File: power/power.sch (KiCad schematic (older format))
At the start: 81 parts, among them J1 Conn_01x02_Female, J2 Conn_01x02_Female, J3 CONN_02X03, J4 Conn_01x06_Female, Q1 BS170, Q10 BS170, Q11 BS170, Q12 BSB014N04LX3, Q2 BS170, Q3 BS170, Q4 BS170, Q5 BS170, Q6 BS170, Q7 BS170, Q8 BS170, Q9 BS170, U1 MAX1648, U2 TPS2592xx, U3 LMC6482, U4 ATSAMD21G18A-AUT

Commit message: added to sch
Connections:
- wire segments 190 -> 187
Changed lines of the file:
@@
 	1    0    0    -1
 $EndComp
-Text Label 10650 1850 0    50   ~ 0
+Text Label 11000 1850 0    50   ~ 0
 T2
 Text Label 9650 1750 2    50   ~ 0
@@
 Text Label 750  6700 2    50   ~ 0
 BAT-
-Text Label 10650 2650 0    50   ~ 0
+Text Label 11000 2650 0    50   ~ 0
 FET1
 Text Label 9650 3050 2    50   ~ 0
 Discharge
-Text Label 10650 2750 0    50   ~ 0
+Text Label 11000 2750 0    50   ~ 0
 FET2
-Text Label 10650 2850 0    50   ~ 0
+Text Label 11000 2850 0    50   ~ 0
 FET3
-Text Label 10650 2950 0    50   ~ 0
+Text Label 11000 2950 0    50   ~ 0
 FET4
 Text Label 9650 3350 2    50   ~ 0
@@
 Connection ~ 6850 6700
 Connection ~ 6850 3950
-Text Label 10650 1950 0    50   ~ 0
+Text Label 11000 1950 0    50   ~ 0
 T1
 $Comp
@@
 	1    0    0    -1
 $EndComp
-Wire Wire Line
-	10150 3850 10250 3850
-Connection ~ 10250 3850
-Wire Wire Line
-	10250 3850 10350 3850
-Connection ~ 10350 3850
-Wire Wire Line
-	10350 3850 10450 3850
-Connection ~ 10450 3850
-Wire Wire Line
-	10450 3850 10700 3850
 Text Label 7150 6700 0    50   ~ 0
 LOAD-
@@
 Text Label 4250 6300 2    50   ~ 0
 SafetySwitch
-Text Label 10650 2050 0    50   ~ 0
+Text Label 11000 2050 0    50   ~ 0
 SafetySwitch
 NoConn ~ 9650 1350
@@
 NoConn ~ 9650 3150
 NoConn ~ 9650 3250
-NoConn ~ 10650 2550
-NoConn ~ 10650 2450
-NoConn ~ 10650 2350
-NoConn ~ 10650 2250
-NoConn ~ 10650 2150
-NoConn ~ 10650 1750
-NoConn ~ 10650 1650
-NoConn ~ 10650 1550
-NoConn ~ 10650 1450
-Wire Wire Line
-	10050 850  10150 850
-Connection ~ 10150 850
-Wire Wire Line
-	10150 850  10250 850
-Connection ~ 10250 850
-Wire Wire Line
-	10250 850  10350 850
-Connection ~ 10350 850
-Wire Wire Line
-	10350 850  10450 850
-Connection ~ 10450 850
-Wire Wire Line
-	10450 850  10650 850
+NoConn ~ 11000 2550
+NoConn ~ 11000 2450
+NoConn ~ 11000 2350
+NoConn ~ 11000 2250
+NoConn ~ 11000 2150
+NoConn ~ 11000 1750
+NoConn ~ 11000 1650
+NoConn ~ 11000 1550
+NoConn ~ 11000 1450
 $Comp
 L power:VCC #PWR0116
@@
 	-1   0    0    1
 $EndComp
+Wire Wire Line
+	10450 3850 10700 3850
+Wire Wire Line
+	10450 850  10650 850
+Wire Wire Line
+	10050 850  10150 850
+Connection ~ 10450 850
+Connection ~ 10150 850
+Wire Wire Line
+	10150 850  10250 850
+Connection ~ 10250 850
+Wire Wire Line
+	10250 850  10350 850
+Connection ~ 10350 850
+Wire Wire Line
+	10350 850  10450 850
 $EndSCHEMATC

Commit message: changed to atmega16
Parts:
- removed C15: C, Capacitor_SMD:C_0805_2012Metric_Pad1.15x1.40mm_HandSolder, symbol Device:C
- removed U4: ATSAMD21G18A-AUT, footprints:TO-263-2-Heatsink, symbol dk_Embedded-Microcontrollers:ATSAMD21G18A-AUT
- added C?: C, Capacitor_SMD:C_0805_2012Metric_Pad1.15x1.40mm_HandSolder, symbol Device:C
- added D?: D_Zener, symbol Device:D_Zener
- added U?: ATMEGA16M1, footprints:TQFP-32_7x7mm_Pitch0.8mm, symbol formula:ATMEGA16M1
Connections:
- net labels added: +3.3V
- wire segments 187 -> 191
- no-connect marks 24 -> 12
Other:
- moved on the sheet: C16, C17, D7, J4, Q10, Q9, R24, R25, R26, R27, R28, R29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

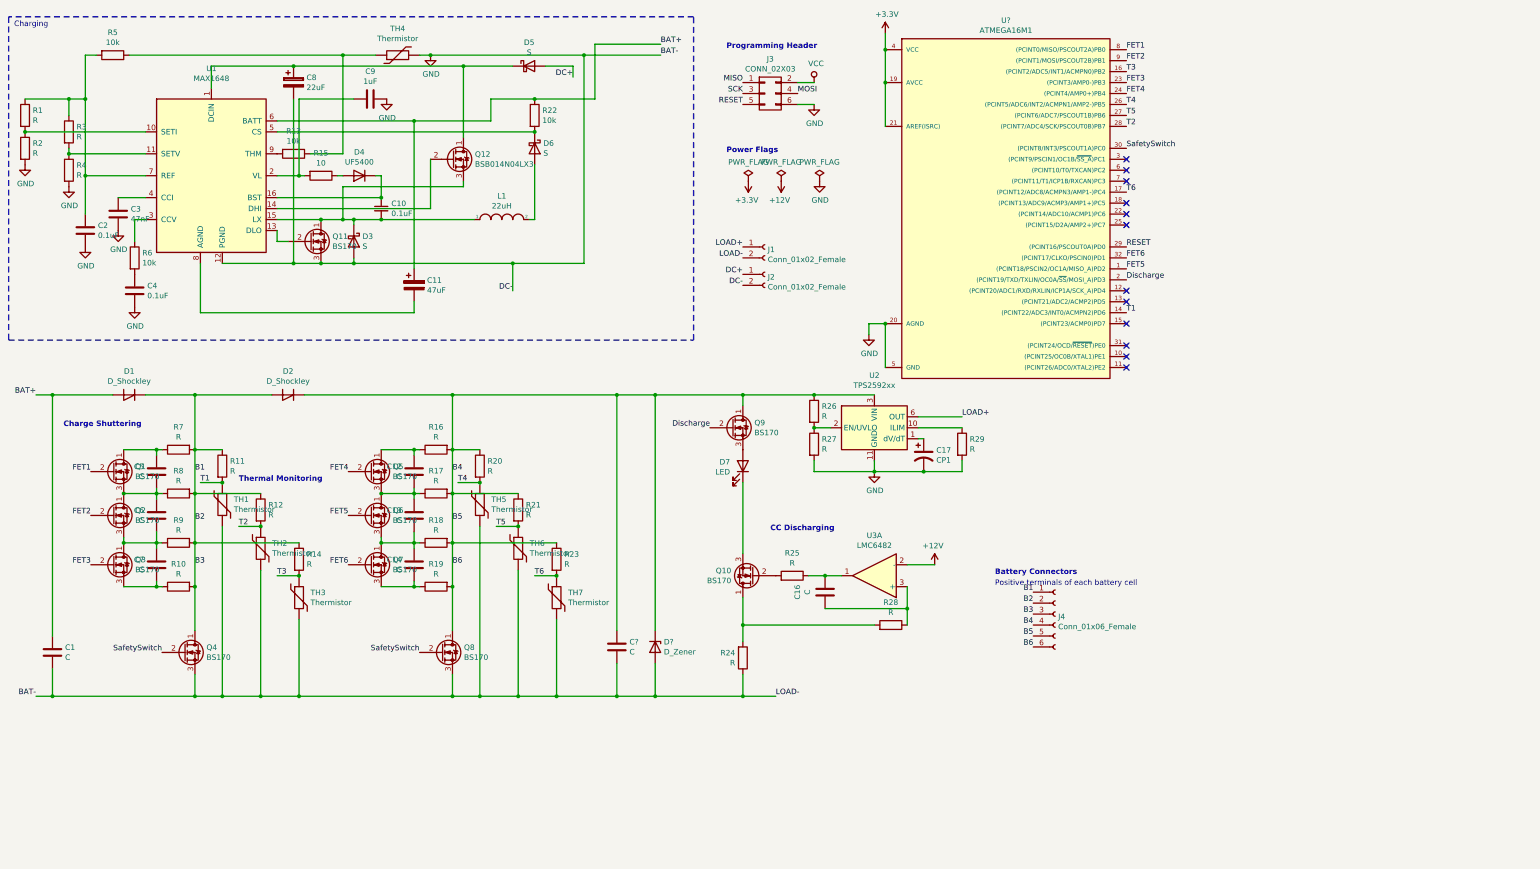
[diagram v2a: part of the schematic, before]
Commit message: Proper atmega configuration with programming header pins
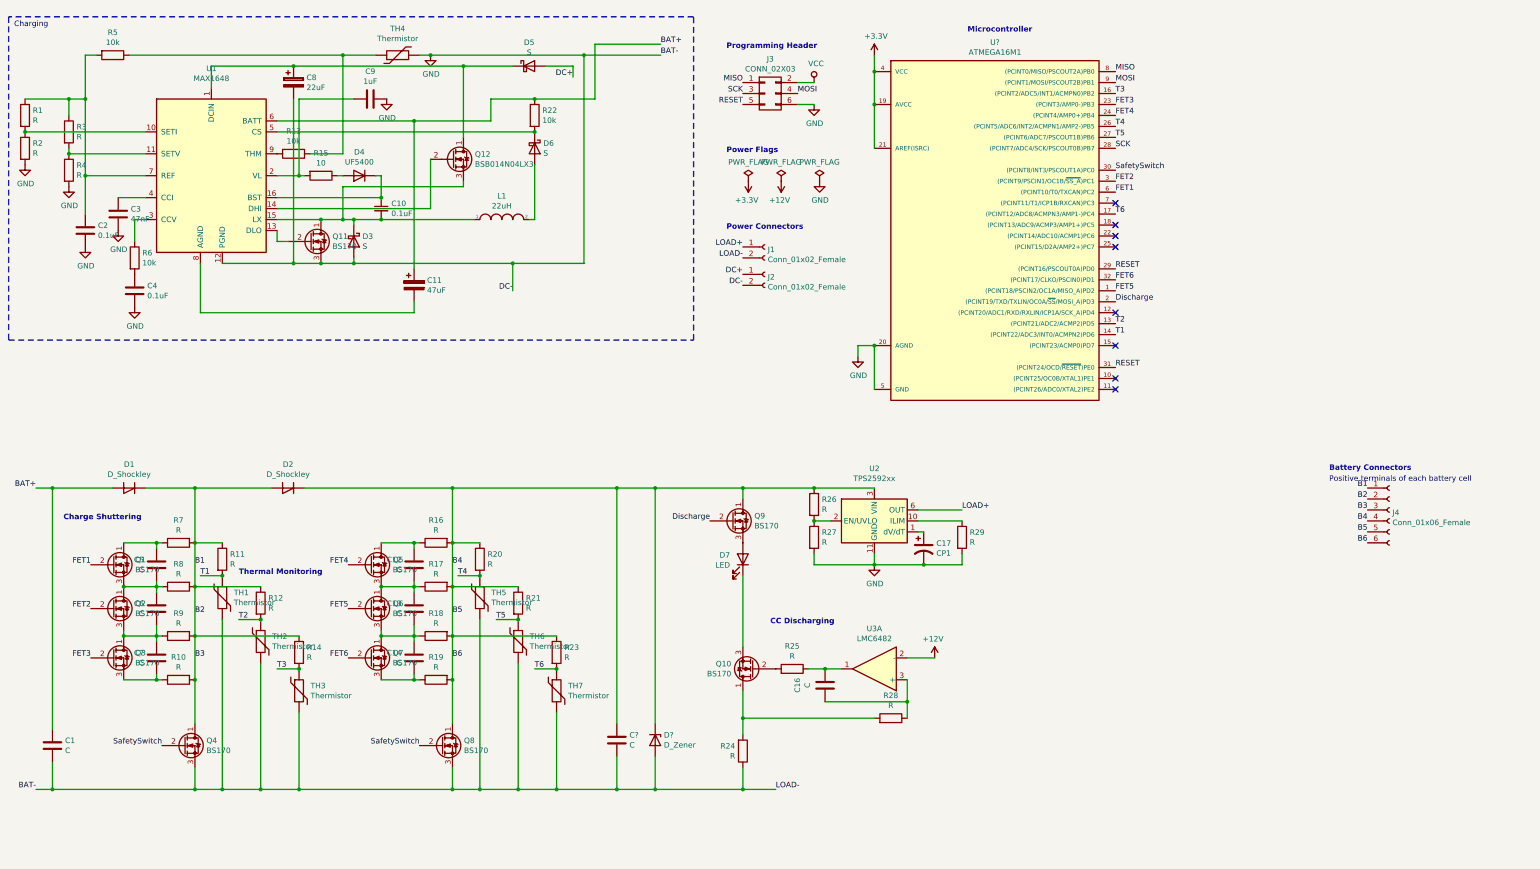
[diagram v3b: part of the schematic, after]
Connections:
- net FET1: now also U?.6 ((PCINT10/T0/TXCAN)PC2); no longer U?.8 ((PCINT0/MISO/PSCOUT2A)PB0)
- net FET2: now also U?.3 ((PCINT9/PSCIN1/OC1B/~SS_A~)PC1); no longer U?.9 ((PCINT1/MOSI/PSCOUT2B)PB1)
- net MISO: now also U?.8 ((PCINT0/MISO/PSCOUT2A)PB0)
- net MOSI: now also U?.9 ((PCINT1/MOSI/PSCOUT2B)PB1)
- net RESET: now also U?.31 ((PCINT24/OCD/~RESET~)PE0)
- net SCK: now also U?.28 ((PCINT7/ADC4/SCK/PSCOUT0B)PB7)
- net T2: now also U?.13 ((PCINT21/ADC2/ACMP2)PD5); no longer U?.28 ((PCINT7/ADC4/SCK/PSCOUT0B)PB7)
- no-connect marks 12 -> 8
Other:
- note added: "Microcontroller"
- note added: "Power Connectors"
- moved on the sheet: C1, C12, C13, C14, C16, C17, C5, C6, C7, C?, D1, D2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

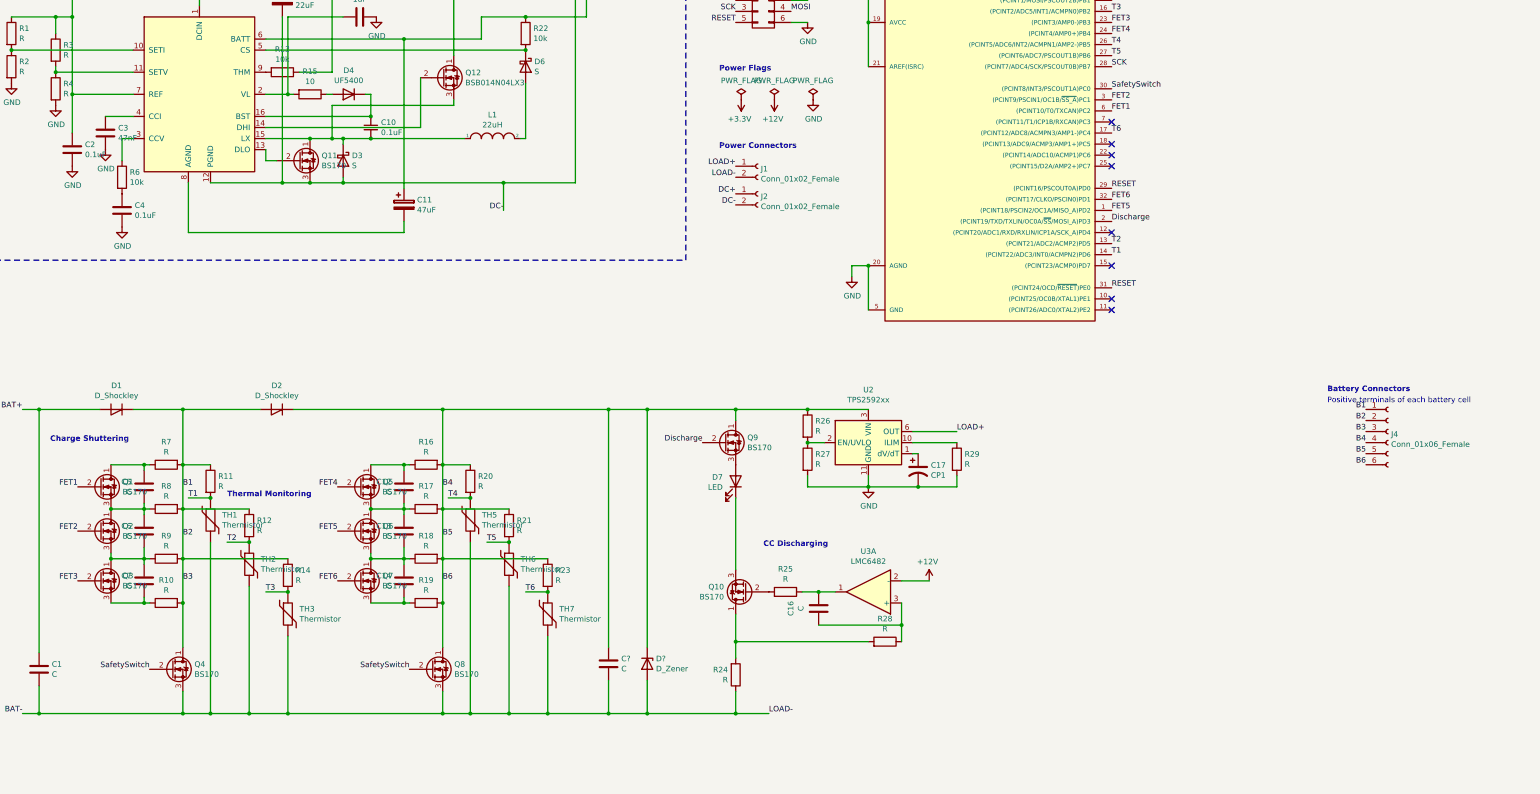
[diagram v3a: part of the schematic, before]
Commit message: negative terminals of bat
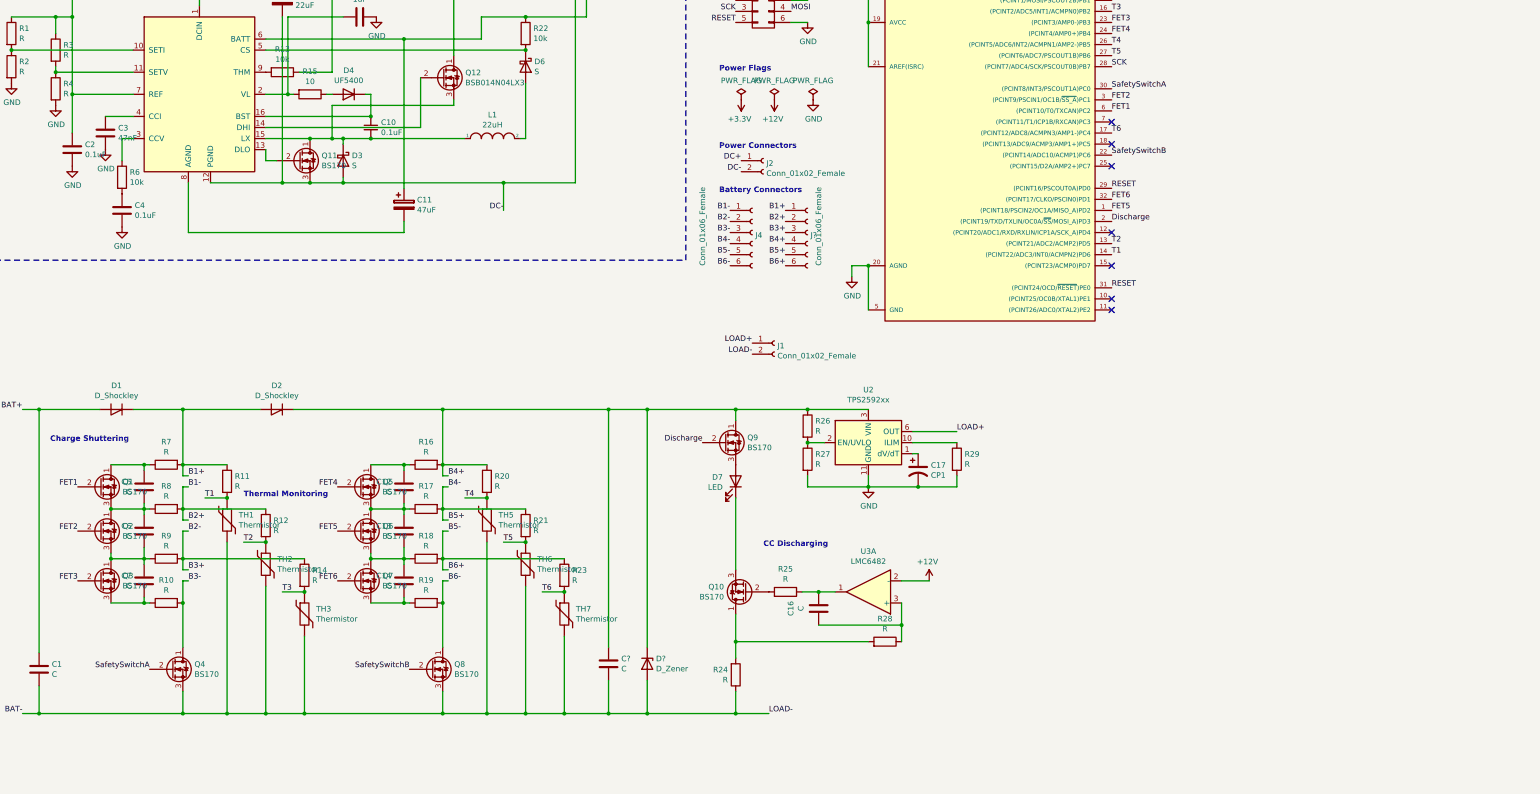
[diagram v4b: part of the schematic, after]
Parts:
- added J?: Conn_01x06_Female, Connector_PinHeader_1.00mm:PinHeader_1x06_P1.00mm_Vertical, symbol Connector:Conn_01x06_Female
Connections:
- net SafetySwitchB: now reaches U?.22 ((PCINT14/ADC10/ACMP1)PC6)
- net SafetySwitchB: now also Q8.2 (G)
- removed net B1: D1.1 (K), D2.2 (A), J4.1 (Pin_1), J4.2 (Pin_2), J4.3 (Pin_3), Q4.1 (D), R10.2, R11.1, R12.1, R14.1, R7.2, R8.2, R9.2
- net B4 renamed B4+
- net B4+: now also J?.4 (Pin_4); no longer J4.4 (Pin_4), J4.5 (Pin_5), J4.6 (Pin_6), Q8.1 (D), R17.2, R18.2, R19.2, R21.1, R23.1
- net SafetySwitch renamed SafetySwitchA
- net SafetySwitchA: no longer Q8.2 (G)
- new net B1+: D1.1 (K), D2.2 (A), J?.1 (Pin_1), R11.1, R7.2
- new net B1-: J4.1 (Pin_1), J?.2 (Pin_2), R12.1, R8.2
- new net B2-: J4.2 (Pin_2), J?.3 (Pin_3), R14.1, R9.2
- new net B3-: J4.3 (Pin_3), Q4.1 (D), R10.2
- new net B4-: J4.4 (Pin_4), J?.5 (Pin_5), R17.2, R21.1
- new net B5-: J4.5 (Pin_5), J?.6 (Pin_6), R18.2, R23.1
- new net B6-: J4.6 (Pin_6), Q8.1 (D), R19.2
- no-connect marks 8 -> 7
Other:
- note removed: "Positive terminals of each battery cell"
- moved on the sheet: J1, J2, J4, R11, R12, R14, R20, R21, R23, TH1, TH2, TH3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
